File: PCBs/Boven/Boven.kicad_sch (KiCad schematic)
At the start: 49 parts, among them SW1 SW_DIP_x08, SW2 SW_DPST_x2

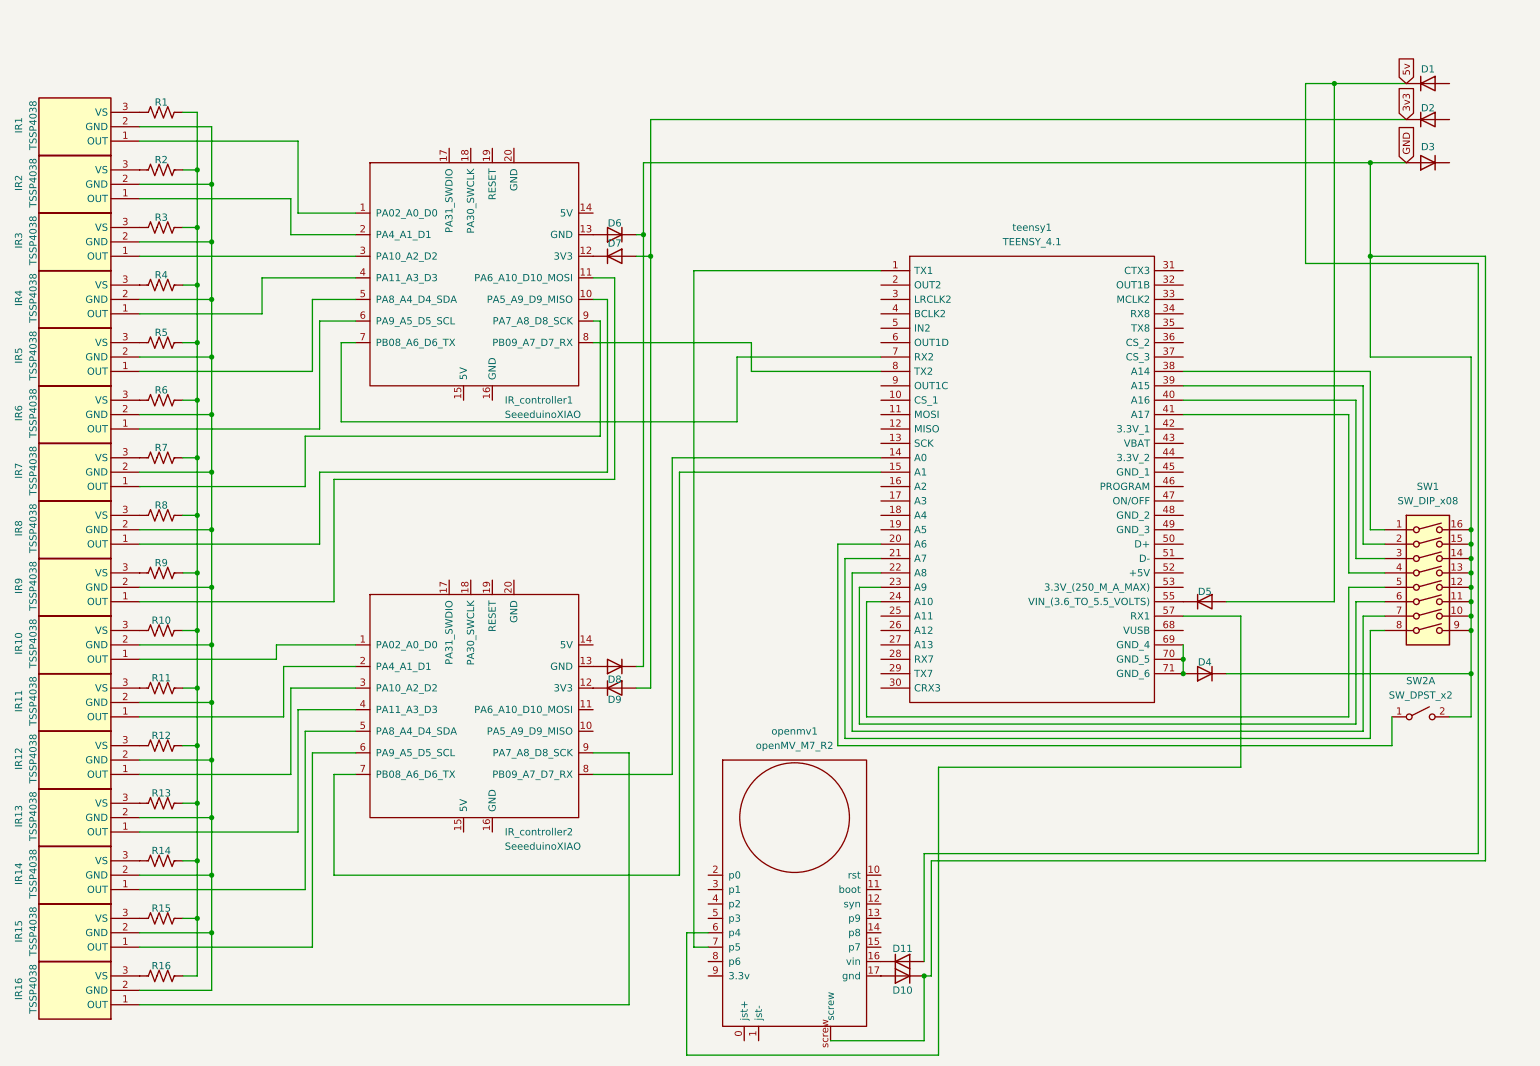
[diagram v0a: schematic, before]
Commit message: PCB schemas
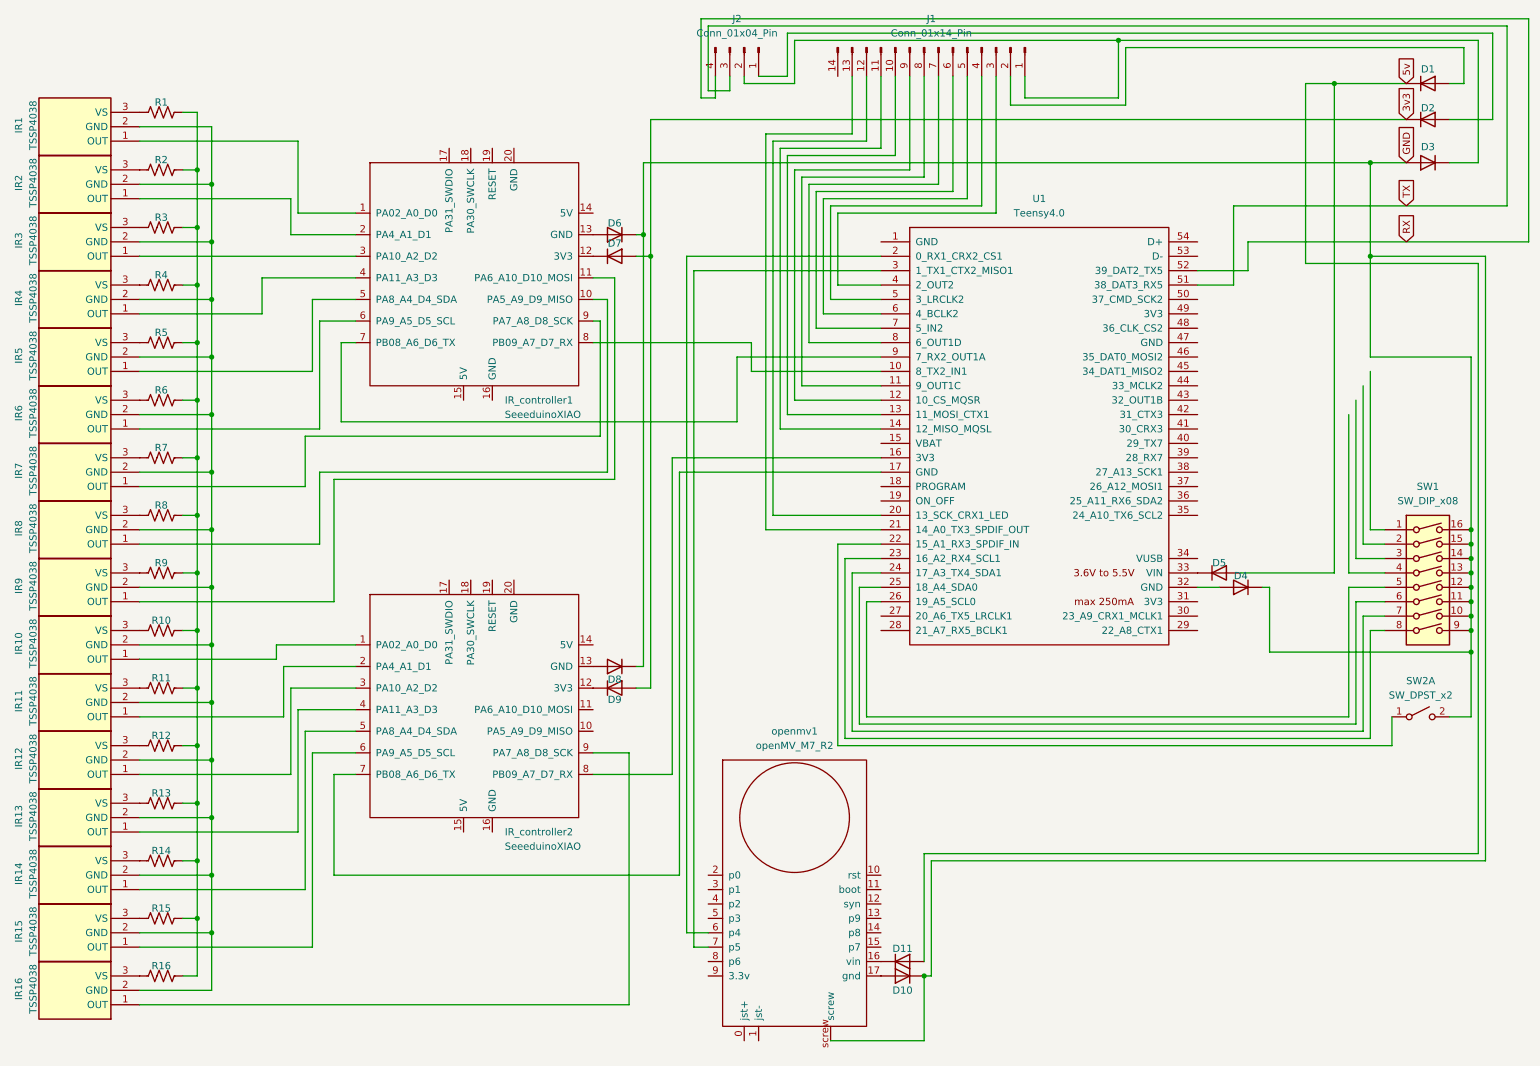
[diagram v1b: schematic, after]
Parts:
- removed teensy1: TEENSY_4.1, TEENSY41, symbol TEENSY_4.1:TEENSY_4.1
- added J1: Conn_01x14_Pin, symbol Connector:Conn_01x14_Pin
- added J2: Conn_01x04_Pin, symbol Connector:Conn_01x04_Pin
- added U1: Teensy4.0, symbol teensy:Teensy4.0
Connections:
- net at D1.2 (A): now also J1.2 (Pin_2)
- net at D4.2 (A): now also U1.32 (GND)
- net at IR_controller2.7 (PB08_A6_D6_TX): now also U1.17 (GND)
- net at IR_controller2.8 (PB09_A7_D7_RX): now also U1.16 (3V3)
- net at IR_controller1.7 (PB08_A6_D6_TX): now also U1.9 (7_RX2_OUT1A)
- net at IR_controller1.8 (PB09_A7_D7_RX): now also U1.10 (8_TX2_IN1)
- net at SW1.5: now also U1.26 (19_A5_SCL0)
- net at SW1.6: now also U1.25 (18_A4_SDA0)
- net at SW1.7: now also U1.24 (17_A3_TX4_SDA1)
- net at SW1.8: now also U1.23 (16_A2_RX4_SCL1)
- net at D2.2 (A): now also J2.1 (Pin_1)
- net at D3.1 (K): now also J1.1 (Pin_1), J2.2 (Pin_2)
- net at openmv1.6 (p4): now also U1.2 (0_RX1_CRX2_CS1)
- net at openmv1.7 (p5): now also U1.3 (1_TX1_CTX2_MISO1)
- net at SW2.1 (A): now also U1.22 (15_A1_RX3_SPDIF_IN)
- net at D5.1 (K): now also U1.33 (VIN)
- new net: J1.10 (Pin_10), U1.13 (11_MOSI_CTX1)
- new net: J1.11 (Pin_11), U1.14 (12_MISO_MQSL)
- new net: J1.12 (Pin_12), U1.20 (13_SCK_CRX1_LED)
- new net: J1.13 (Pin_13), U1.21 (14_A0_TX3_SPDIF_OUT)
- new net: J1.3 (Pin_3), U1.4 (2_OUT2)
- new net: J1.4 (Pin_4), U1.5 (3_LRCLK2)
- new net: J1.5 (Pin_5), U1.6 (4_BCLK2)
- new net: J1.6 (Pin_6), U1.7 (5_IN2)
- new net: J1.7 (Pin_7), U1.8 (6_OUT1D)
- new net: J1.8 (Pin_8), U1.11 (9_OUT1C)
- new net: J1.9 (Pin_9), U1.12 (10_CS_MQSR)
- new net RX: J2.4 (Pin_4), U1.52 (39_DAT2_TX5)
- new net TX: J2.3 (Pin_3), U1.51 (38_DAT3_RX5)
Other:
- company: (none) -> Robotica Mendelcollege
- title: (none) -> Bovenste PCB schema
- moved on the sheet: D4, D5
